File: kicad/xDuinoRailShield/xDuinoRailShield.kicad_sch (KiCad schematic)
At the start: 0 parts

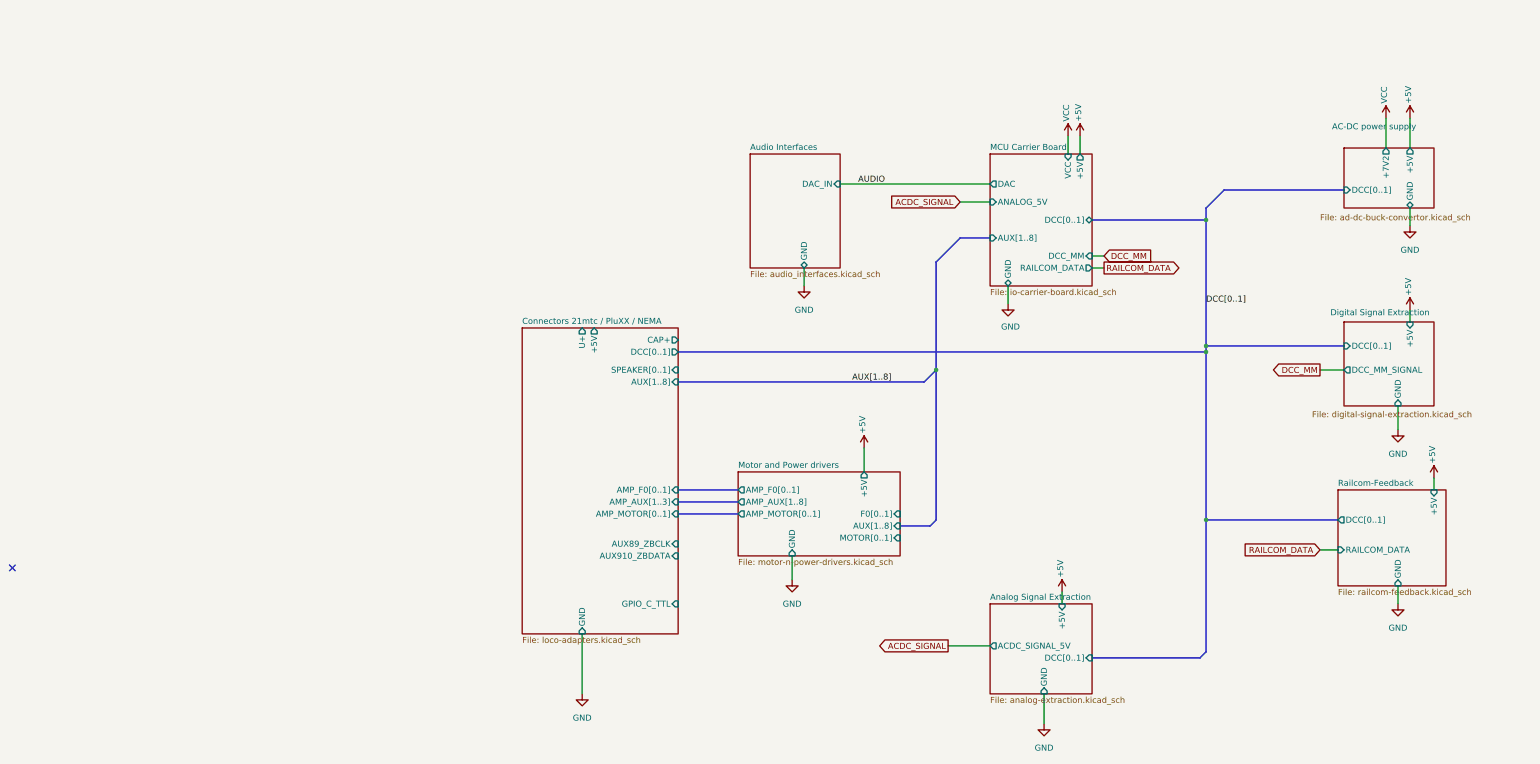
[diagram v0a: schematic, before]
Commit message: Draft of loco decoder
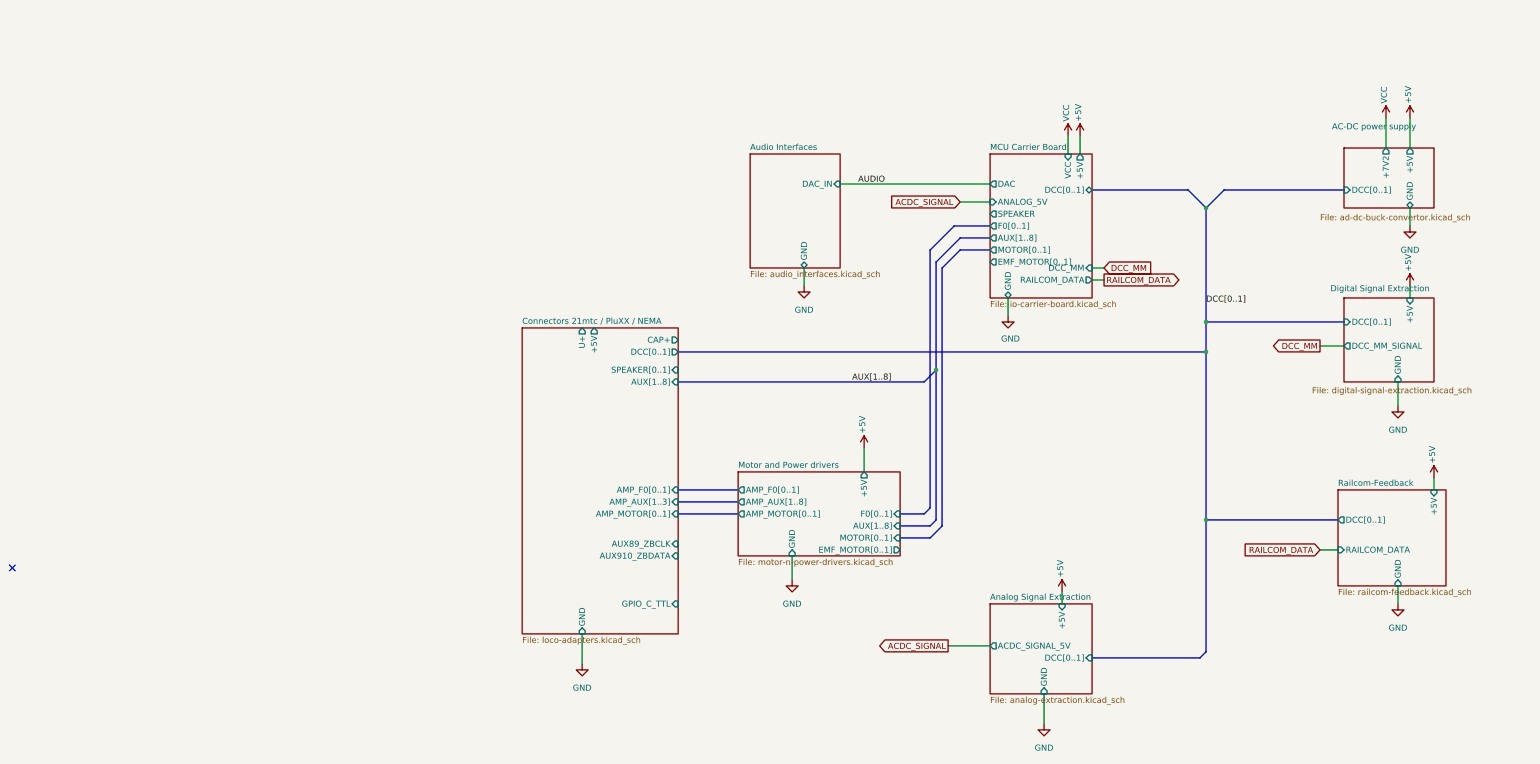
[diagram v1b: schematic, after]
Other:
- sheet MCU Carrier Board ports: added EMF_MOTOR[0..1], F0[0..1], MOTOR[0..1], SPEAKER; removed none
- sheet Motor and Power drivers ports: added EMF_MOTOR[0..1]; removed none

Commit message: A lot of fixes
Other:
- added sheet Special-I2C-Sensors (i2c-sensors.kicad_sch)
- sheet AC-DC power supply ports: added U+; removed none
- sheet Audio Interfaces ports: added U+; removed none
- sheet Connectors 21mtc / PluXX / NEMA ports: added AMP_AUX[1..7], AMP_FUNC[0..1]; removed AMP_AUX[1..3], AMP_F0[0..1]
- sheet MCU Carrier Board ports: added +3V3, FUNC[0..1], I2C[0..1], SPEAKER[0..1]; removed F0[0..1], SPEAKER
- sheet Motor and Power drivers ports: added AMP_FUNC[0..1], FUNC[0..1], U+; removed AMP_F0[0..1], F0[0..1]

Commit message: Refactoring & Sound
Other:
- sheet Audio Interfaces ports: added I2C[0..1], SPEAKER[0..1], SUSI_CLOCK, SUSI_DATA, SUSI_TRIGGER; removed none
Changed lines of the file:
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@@
+	)
+	(junction
+		(at 97.79 33.02)
+		(diameter 0)
+		(color 0 0 0 0)
 	)
 	(junction
@@
 	(bus
 		(pts
+			(xy 71.12 88.9) (xy 63.5 88.9)
+		)
+		(stroke
+			(width 0)
+			(type default)
+		)
+	)
+	(bus
+		(pts
 			(xy 116.84 63.5) (xy 116.84 118.11)
 		)
@@
 		)
 	)
-	(bus
-		(pts
-			(xy 115.57 88.9) (xy 115.57 55.88)
-		)
-		(stroke
-			(width 0)
-			(type default)
-		)
-	)
 	(wire
 		(pts
@@
 	(bus
 		(pts
-			(xy 64.77 33.02) (xy 114.3 33.02)
+			(xy 64.77 33.02) (xy 97.79 33.02)
 		)
 		(stroke
@@
 	(bus
 		(pts
+			(xy 71.12 88.9) (xy 71.12 69.85)
+		)
+		(stroke
+			(width 0)
+			(type default)
+		)
+	)
+	(bus
+		(pts
 			(xy 114.3 45.72) (xy 129.54 45.72)
 		)
@@
 	(bus
 		(pts
-			(xy 115.57 55.88) (xy 129.54 55.88)
-		)
-		(stroke
-			(width 0)
-			(type default)
-		)
-	)
-	(bus
-		(pts
 			(xy 175.26 54.61) (xy 171.45 50.8)
 		)
@@
 		)
 	)
-	(bus
-		(pts
-			(xy 63.5 88.9) (xy 115.57 88.9)
-		)
-		(stroke
-			(width 0)
-			(type default)
-		)
-	)
 	(wire
 		(pts
@@
 	(bus
 		(pts
+			(xy 97.79 33.02) (xy 114.3 33.02)
+		)
+		(stroke
+			(width 0)
+			(type default)
+		)
+	)
+	(bus
+		(pts
+			(xy 71.12 69.85) (xy 73.66 69.85)
+		)
+		(stroke
+			(width 0)
+			(type default)
+		)
+	)
+	(bus
+		(pts
 			(xy 175.26 54.61) (xy 175.26 78.74)
 		)
@@
 		)
 	)
+	(bus
+		(pts
+			(xy 97.79 33.02) (xy 97.79 58.42)
+		)
+		(stroke
+			(width 0)
+			(type default)
+		)
+	)
 	(wire
 		(pts
@@
 		(pts
 			(xy 123.19 63.5) (xy 119.38 67.31)
+		)
+		(stroke
+			(width 0)
+			(type default)
+		)
+	)
+	(bus
+		(pts
+			(xy 97.79 58.42) (xy 88.9 58.42)
 		)
 		(stroke
@@
 				)
 				(justify left top)
+				(hide yes)
 			)
 		)
@@
 			)
 		)
+		(pin "SUSI_CLOCK" input
+			(at 88.9 66.04 0)
+			(effects
+				(font
+					(size 1.27 1.27)
+				)
+				(justify right)
+			)
+		)
+		(pin "SUSI_DATA" input
+			(at 88.9 63.5 0)
+			(effects
+				(font
+					(size 1.27 1.27)
+				)
+				(justify right)
+			)
+		)
+		(pin "SUSI_TRIGGER" input
+			(at 88.9 60.96 0)
+			(effects
+				(font
+					(size 1.27 1.27)
+				)
+				(justify right)
+			)
+		)
+		(pin "I2C[0..1]" bidirectional
+			(at 88.9 58.42 0)
+			(effects
+				(font
+					(size 1.27 1.27)
+				)
+				(justify right)
+			)
+		)
+		(pin "SPEAKER[0..1]" output
+			(at 73.66 69.85 180)
+			(effects
+				(font
+					(size 1.27 1.27)
+				)
+				(justify left)
+			)
+		)

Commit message: More refactoring
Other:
- sheet AC-DC power supply ports: added +3V3; removed none
- sheet Connectors 21mtc / PluXX / NEMA ports: added none; removed +5V
- sheet Motor and Power drivers ports: added +3V3; removed +5V
- sheet Railcom-Feedback ports: added +3V3; removed +5V
